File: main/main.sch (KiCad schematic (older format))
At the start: 6 parts

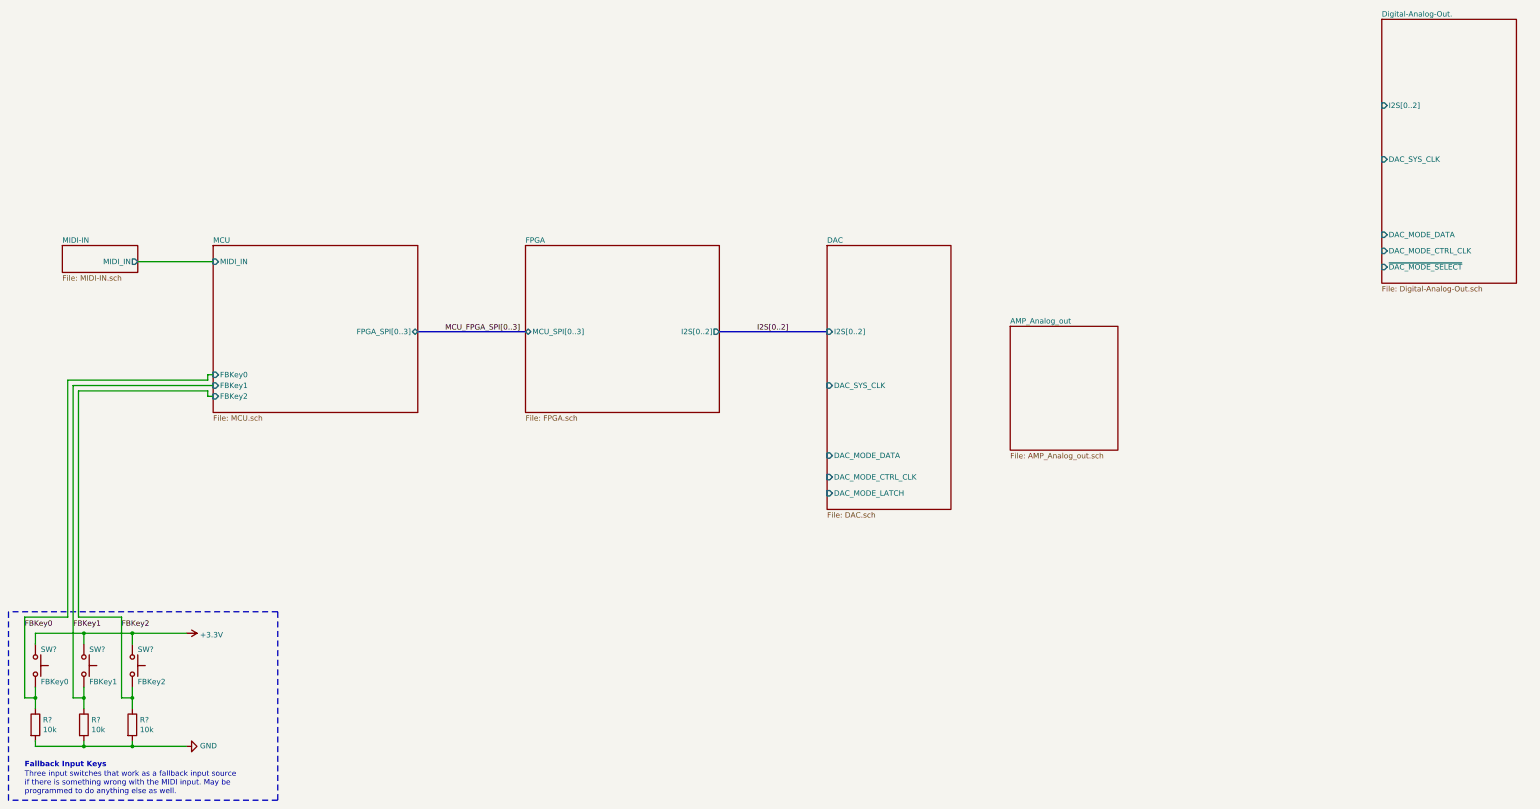
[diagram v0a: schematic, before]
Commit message: Remove old DAC files. Connect amplifier to audio out
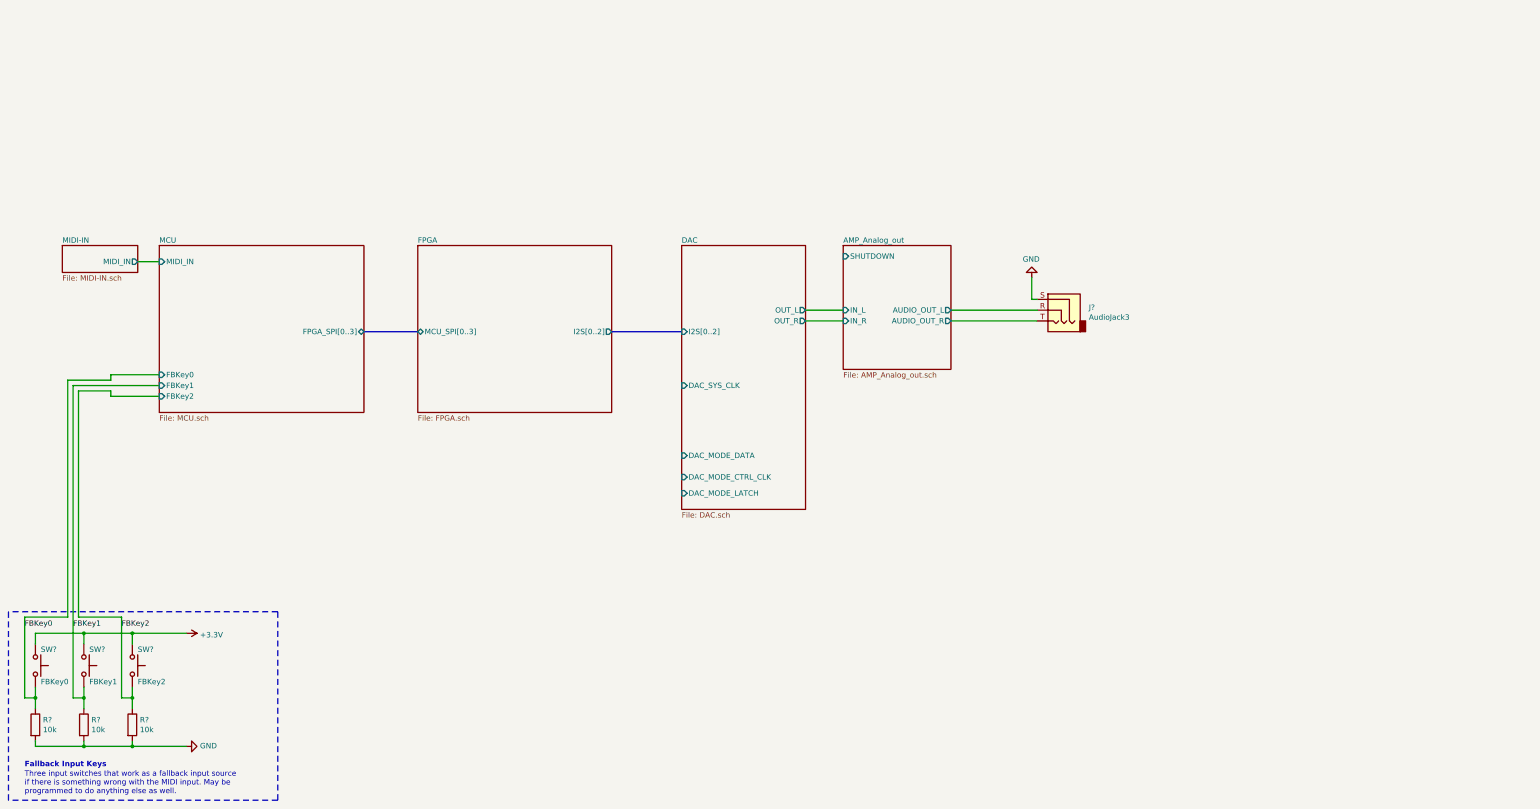
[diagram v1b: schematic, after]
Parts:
- added J?: AudioJack3, symbol Connector:AudioJack3
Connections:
- net GND: now also J?.S
- new net AMP_Analog_out/AUDIO_OUT_L: J?.R
- new net AMP_Analog_out/AUDIO_OUT_R: J?.T
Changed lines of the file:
@@
 $Descr A4 11693 8268
 encoding utf-8
-Sheet 1 7
+Sheet 1 6
 Title "Synthesizer"
 Date "2021-09-06"
@@
 $EndSheet
 $Sheet
-S 13300 450  1250 2450
-U 61417224
-F0 "Digital-Analog-Out." 50
-F1 "Digital-Analog-Out.sch" 50
-F2 "~DAC_MODE_SELECT" I L 13300 2750 50
-F3 "DAC_MODE_CTRL_CLK" I L 13300 2600 50
-F4 "DAC_MODE_DATA" I L 13300 2450 50
-F5 "DAC_SYS_CLK" I L 13300 1750 50
-F6 "I2S[0..2]" I L 13300 1250 50
-$EndSheet
-Text Label 7500 3350 0    50   ~ 0
-I2S[0..2]
-$Sheet
-S 5350 2550 1800 1550
+S 4350 2550 1800 1550
 U 613F0EEF
 F0 "FPGA" 50
 F1 "FPGA.sch" 50
-F2 "I2S[0..2]" O R 7150 3350 50
-F3 "MCU_SPI[0..3]" B L 5350 3350 50
-$EndSheet
-Text Label 5300 3350 2    50   ~ 0
-MCU_FPGA_SPI[0..3]
-$Sheet
-S 2450 2550 1900 1550
+F2 "I2S[0..2]" O R 6150 3350 50
+F3 "MCU_SPI[0..3]" B L 4350 3350 50
+$EndSheet
+$Sheet
+S 1950 2550 1900 1550
 U 6139E7E0
 F0 "MCU" 50
 F1 "MCU.sch" 50
-F2 "MIDI_IN" I L 2450 2700 50
-F3 "FPGA_SPI[0..3]" B R 4350 3350 50
-F4 "FBKey0" I L 2450 3750 50
-F5 "FBKey1" I L 2450 3850 50
-F6 "FBKey2" I L 2450 3950 50
-$EndSheet
-Wire Wire Line
-	1750 2700 2450 2700
+F2 "MIDI_IN" I L 1950 2700 50
+F3 "FPGA_SPI[0..3]" B R 3850 3350 50
+F4 "FBKey0" I L 1950 3750 50
+F5 "FBKey1" I L 1950 3850 50
+F6 "FBKey2" I L 1950 3950 50
+$EndSheet
+Wire Wire Line
+	1750 2700 1950 2700
 Wire Bus Line
-	4350 3350 5350 3350
+	3850 3350 4350 3350
 Wire Bus Line
-	7150 3350 8150 3350
-$Sheet
-S 8150 2550 1150 2450
+	6150 3350 6800 3350
+$Sheet
+S 6800 2550 1150 2450
 U 61496F7B
 F0 "DAC" 50
 F1 "DAC.sch" 50
-F2 "I2S[0..2]" I L 8150 3350 50
-F3 "DAC_SYS_CLK" I L 8150 3850 50
-F4 "DAC_MODE_DATA" I L 8150 4500 50
-F5 "DAC_MODE_CTRL_CLK" I L 8150 4700 50
-F6 "DAC_MODE_LATCH" I L 8150 4850 50
+F2 "I2S[0..2]" I L 6800 3350 50
+F3 "DAC_SYS_CLK" I L 6800 3850 50
+F4 "DAC_MODE_DATA" I L 6800 4500 50
+F5 "DAC_MODE_CTRL_CLK" I L 6800 4700 50
+F6 "DAC_MODE_LATCH" I L 6800 4850 50
+F7 "OUT_L" O R 7950 3150 50
+F8 "OUT_R" O R 7950 3250 50
 $EndSheet
 $Comp
@@
 	700  6000 700  6750
 Wire Wire Line
-	1150 3850 2450 3850
+	1150 3850 1950 3850
 Wire Wire Line
 	1150 3850 1150 6750
@@
 	3050 5950 550  5950
 Wire Wire Line
-	1100 3800 2400 3800
-Wire Wire Line
-	1200 3900 2400 3900
+	1100 3800 1500 3800
+Wire Wire Line
+	1200 3900 1500 3900
 Wire Wire Line
 	1100 6000 1100 3800
@@
 	1600 6000 1200 6000
 Wire Wire Line
-	2400 3900 2400 3950
-Wire Wire Line
-	2400 3950 2450 3950
-Wire Wire Line
-	2400 3800 2400 3750
-Wire Wire Line
-	2400 3750 2450 3750
-$Sheet
-S 9850 3300 1000 1150
+	1500 3900 1500 3950
+Wire Wire Line
+	1500 3950 1950 3950
+Wire Wire Line
+	1500 3800 1500 3750
+Wire Wire Line
+	1500 3750 1950 3750
+$Sheet
+S 8300 2550 1000 1150
 U 61447D69
 F0 "AMP_Analog_out" 50
 F1 "AMP_Analog_out.sch" 50
-$EndSheet
+F2 "IN_L" I L 8300 3150 50
+F3 "IN_R" I L 8300 3250 50
+F4 "SHUTDOWN" I L 8300 2650 50
+F5 "AUDIO_OUT_L" O R 9300 3150 50
+F6 "AUDIO_OUT_R" O R 9300 3250 50
+$EndSheet
+Wire Wire Line
+	7950 3250 8300 3250
+Wire Wire Line
+	7950 3150 8300 3150
+$Comp
+L Connector:AudioJack3 J?
+U 1 1 614686B4
+P 10300 3150
+F 0 "J?" H 10020 3175 50  0000 R CNN
+F 1 "AudioJack3" H 10020 3084 50  0000 R CNN
+F 2 "" H 10300 3150 50  0001 C CNN
+F 3 "~" H 10300 3150 50  0001 C CNN
+	1    10300 3150
+	-1   0    0    -1
+$EndComp
+$Comp
+L power:GND #PWR?
+U 1 1 614690FB
+P 10050 2850
+F 0 "#PWR?" H 10050 2600 50  0001 C CNN
+F 1 "GND" H 10055 2677 50  0000 C CNN
+F 2 "" H 10050 2850 50  0001 C CNN
+F 3 "" H 10050 2850 50  0001 C CNN
+	1    10050 2850
+	-1   0    0    1
+$EndComp
+Wire Wire Line
+	10050 3050 10100 3050
+Wire Wire Line
+	10050 2850 10050 3050
+Wire Wire Line
+	9300 3150 10100 3150
+Wire Wire Line
+	9300 3250 10100 3250
 $EndSCHEMATC

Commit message: Set up switching regulator circuits.
We only use half of the switching regulator that generates the 1V0
voltage. I'm not sure if the half not being used is connected correctly.
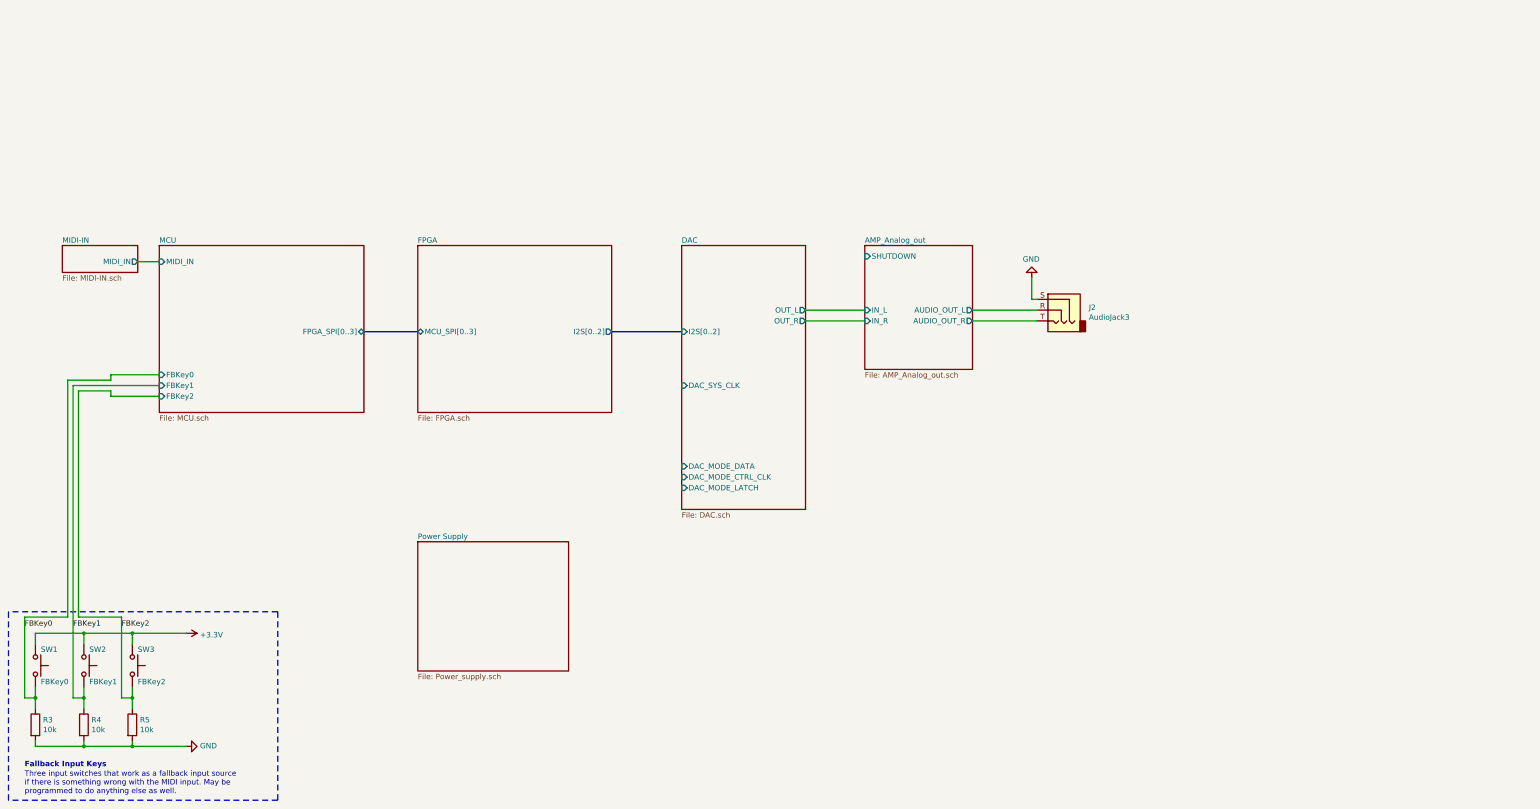
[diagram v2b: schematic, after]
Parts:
- gave numbers to parts that had none: 7
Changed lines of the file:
@@
 $Descr A4 11693 8268
 encoding utf-8
-Sheet 1 6
+Sheet 1 7
 Title "Synthesizer"
 Date "2021-09-06"
@@
 F2 "I2S[0..2]" I L 6800 3350 50
 F3 "DAC_SYS_CLK" I L 6800 3850 50
-F4 "DAC_MODE_DATA" I L 6800 4500 50
+F4 "DAC_MODE_DATA" I L 6800 4600 50
 F5 "DAC_MODE_CTRL_CLK" I L 6800 4700 50
-F6 "DAC_MODE_LATCH" I L 6800 4850 50
+F6 "DAC_MODE_LATCH" I L 6800 4800 50
 F7 "OUT_L" O R 7950 3150 50
 F8 "OUT_R" O R 7950 3250 50
 $EndSheet
 $Comp
-L Switch:SW_Push SW?
+L Switch:SW_Push SW1
 U 1 1 6145369A
 P 800 6450
-F 0 "SW?" V 650 6500 50  0000 L CNN
+F 0 "SW1" V 650 6500 50  0000 L CNN
 F 1 "FBKey0" V 950 6500 50  0000 L CNN
 F 2 "" H 800 6650 50  0001 C CNN
@@
 $EndComp
 $Comp
-L Device:R R?
+L Device:R R3
 U 1 1 61453C7F
 P 800 7000
-F 0 "R?" H 870 7046 50  0000 L CNN
+F 0 "R3" H 870 7046 50  0000 L CNN
 F 1 "10k" H 870 6955 50  0000 L CNN
 F 2 "" V 730 7000 50  0001 C CNN
@@
 $EndComp
 $Comp
-L Switch:SW_Push SW?
+L Switch:SW_Push SW2
 U 1 1 6145516D
 P 1250 6450
-F 0 "SW?" V 1100 6500 50  0000 L CNN
+F 0 "SW2" V 1100 6500 50  0000 L CNN
 F 1 "FBKey1" V 1400 6500 50  0000 L CNN
 F 2 "" H 1250 6650 50  0001 C CNN
@@
 $EndComp
 $Comp
-L Device:R R?
+L Device:R R4
 U 1 1 61455173
 P 1250 7000
-F 0 "R?" H 1320 7046 50  0000 L CNN
+F 0 "R4" H 1320 7046 50  0000 L CNN
 F 1 "10k" H 1320 6955 50  0000 L CNN
 F 2 "" V 1180 7000 50  0001 C CNN
@@
 $EndComp
 $Comp
-L Switch:SW_Push SW?
+L Switch:SW_Push SW3
 U 1 1 61455E9E
 P 1700 6450
-F 0 "SW?" V 1550 6500 50  0000 L CNN
+F 0 "SW3" V 1550 6500 50  0000 L CNN
 F 1 "FBKey2" V 1850 6500 50  0000 L CNN
 F 2 "" H 1700 6650 50  0001 C CNN
@@
 $EndComp
 $Comp
-L Device:R R?
+L Device:R R5
 U 1 1 61455EA4
 P 1700 7000
-F 0 "R?" H 1770 7046 50  0000 L CNN
+F 0 "R5" H 1770 7046 50  0000 L CNN
 F 1 "10k" H 1770 6955 50  0000 L CNN
 F 2 "" V 1630 7000 50  0001 C CNN
@@
 	1700 6150 2200 6150
 $Comp
-L power:+3.3V #PWR?
+L power:+3.3V #PWR0101
 U 1 1 61456654
 P 2200 6150
-F 0 "#PWR?" H 2200 6000 50  0001 C CNN
+F 0 "#PWR0101" H 2200 6000 50  0001 C CNN
 F 1 "+3.3V" V 2215 6278 50  0000 L CNN
 F 2 "" H 2200 6150 50  0001 C CNN
@@
 $EndComp
 $Comp
-L power:GND #PWR?
+L power:GND #PWR0102
 U 1 1 61457106
 P 2200 7200
-F 0 "#PWR?" H 2200 6950 50  0001 C CNN
+F 0 "#PWR0102" H 2200 6950 50  0001 C CNN
 F 1 "GND" V 2205 7072 50  0000 R CNN
 F 2 "" H 2200 7200 50  0001 C CNN
@@
 	1500 3750 1950 3750
 $Sheet
-S 8300 2550 1000 1150
+S 8500 2550 1000 1150
 U 61447D69
 F0 "AMP_Analog_out" 50
 F1 "AMP_Analog_out.sch" 50
-F2 "IN_L" I L 8300 3150 50
-F3 "IN_R" I L 8300 3250 50
-F4 "SHUTDOWN" I L 8300 2650 50
-F5 "AUDIO_OUT_L" O R 9300 3150 50
-F6 "AUDIO_OUT_R" O R 9300 3250 50
-$EndSheet
-Wire Wire Line
-	7950 3250 8300 3250
-Wire Wire Line
-	7950 3150 8300 3150
-$Comp
-L Connector:AudioJack3 J?
+F2 "IN_L" I L 8500 3150 50
+F3 "IN_R" I L 8500 3250 50
+F4 "SHUTDOWN" I L 8500 2650 50
+F5 "AUDIO_OUT_L" O R 9500 3150 50
+F6 "AUDIO_OUT_R" O R 9500 3250 50
+$EndSheet
+Wire Wire Line
+	7950 3250 8500 3250
+Wire Wire Line
+	7950 3150 8500 3150
+$Comp
+L Connector:AudioJack3 J2
 U 1 1 614686B4
 P 10300 3150
-F 0 "J?" H 10020 3175 50  0000 R CNN
+F 0 "J2" H 10020 3175 50  0000 R CNN
 F 1 "AudioJack3" H 10020 3084 50  0000 R CNN
 F 2 "" H 10300 3150 50  0001 C CNN
@@
 $EndComp
 $Comp
-L power:GND #PWR?
+L power:GND #PWR0103
 U 1 1 614690FB
 P 10050 2850
-F 0 "#PWR?" H 10050 2600 50  0001 C CNN
+F 0 "#PWR0103" H 10050 2600 50  0001 C CNN
 F 1 "GND" H 10055 2677 50  0000 C CNN
 F 2 "" H 10050 2850 50  0001 C CNN
@@
 	10050 2850 10050 3050
 Wire Wire Line
-	9300 3150 10100 3150
-Wire Wire Line
-	9300 3250 10100 3250
+	9500 3150 10100 3150
+Wire Wire Line
+	9500 3250 10100 3250
+$Sheet
+S 4350 5300 1400 1200
+U 61483B8A
+F0 "Power Supply" 50
+F1 "Power_supply.sch" 50
+$EndSheet
 $EndSCHEMATC

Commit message: Continue wiring of the MCU
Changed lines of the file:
@@
-$EndSheet
-$Sheet
-S 4350 2550 1800 1550
-U 613F0EEF
-F0 "FPGA" 50
-F1 "FPGA.sch" 50
-F2 "I2S[0..2]" O R 6150 3350 50
-F3 "MCU_SPI[0..3]" B L 4350 3350 50
 $EndSheet
 $Sheet
@@
 	9500 3250 10100 3250
 $Sheet
-S 4350 5300 1400 1200
+S 1050 800  1400 1200
 U 61483B8A
 F0 "Power Supply" 50
 F1 "Power_supply.sch" 50
 $EndSheet
+$Sheet
+S 4350 2550 1800 1550
+U 613F0EEF
+F0 "FPGA" 50
+F1 "FPGA.sch" 50
+F2 "I2S[0..2]" O R 6150 3350 50
+F3 "MCU_SPI[0..3]" B L 4350 3350 50
+$EndSheet
 $EndSCHEMATC

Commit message: Be consistent with capacitor values (always use F)
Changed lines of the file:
@@
 F2 "I2S[0..2]" O R 6150 3350 50
 F3 "MCU_SPI[0..3]" B L 4350 3350 50
+F4 "done" O L 4350 3850 50
+F5 "program_b" I L 4350 3950 50
 $EndSheet
 $EndSCHEMATC

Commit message: Some tweaks
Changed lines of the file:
@@
 encoding utf-8
 Sheet 1 7
-Title "Synthesizer"
-Date "2021-09-06"
+Title "MIDI Audio Box"
+Date "2021-09-21"
 Rev "v01"
 Comp ""
 Comment1 ""
 Comment2 ""
-Comment3 ""
+Comment3 "Authors: Iver Håkonsen, Halvor Bjørstad"
 Comment4 "TDT4295 Computer Design Project"
 $EndDescr
@@
 F5 "FBKey1" I L 1950 3850 50
 F6 "FBKey2" I L 1950 3950 50
+F7 "external_clock_out" O R 3850 3700 50
 $EndSheet
 Wire Wire Line
